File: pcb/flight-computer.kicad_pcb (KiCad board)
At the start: 4 copper layers, 74 parts, among them J1 MicroSD Slot, J2 USB_C_Receptacle_USB2.0_16P, J3 SMA_Coax, J4 Conn_01x02, J5 ARM, SW1 SW_Push, SW2 SW_Push, U1 RP2040, U10 TPS2116DRL, U11 RN2903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

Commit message: Filled out the BOM for the schematic. Consolidated some components and changed footprint sizes.
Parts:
- removed C1, C2: 15p, Capacitor_SMD:C_0402_1005Metric
- removed C10, C11, C12, C13, C14, C15, C16, C17, C19, C20, C23, C24, C25, C26, C3, C5, C6, C8, C9: 100n, Capacitor_SMD:C_0201_0603Metric
- removed C18, C30: 10u, Capacitor_SMD:C_0805_2012Metric
- removed C21: 220n, Capacitor_SMD:C_0603_1608Metric
- removed C22, C31: 4u7, Capacitor_SMD:C_0603_1608Metric
- removed C27, C4: 2u2, Capacitor_SMD:C_0603_1608Metric
- removed C28, C29, C32, C7: 1u, Capacitor_SMD:C_0603_1608Metric
- removed D1: RED LED, LED_SMD:LED_0805_2012Metric
- removed D2, D3, D4: GREEN LED, LED_SMD:LED_0805_2012Metric
- removed J1: MicroSD Slot, microsd:GCT_MEM2067-02-180-00-A_REVB
- removed J2: USB_C_Receptacle_USB2.0_16P, Connector_USB:USB_C_Receptacle_GCT_USB4105-xx-A_16P_TopMnt_Horizontal
- removed J3: SMA_Coax, Connector_Coaxial:SMA_Molex_73251-1153_EdgeMount_Horizontal
- removed J4: Conn_01x02, Connector_JST:JST_PH_S2B-PH-K_1x02_P2.00mm_Horizontal
- removed J5: ARM, TerminalBlock_Phoenix:TerminalBlock_Phoenix_MKDS-1,5-2_1x02_P5.00mm_Horizontal
- removed L1: 2u2, Inductor_SMD:L_0805_2012Metric
- removed LS1: ACTIVE BUZZER, buzzer:XDCR_AI-1223-TWT-3V-2-R
- removed R1: 11k, Resistor_SMD:R_0201_0603Metric
- removed R10, R11: 5k1, Resistor_SMD:R_0201_0603Metric
- removed R12, R13, R14, R17, R2, R9: 1k, Resistor_SMD:R_0201_0603Metric
- removed R15: 150R, Resistor_SMD:R_0201_0603Metric
- removed R16: 10k, Resistor_SMD:R_0201_0603Metric
- removed R3, R4, R5, R6: 2k2, Resistor_SMD:R_0201_0603Metric
- removed R7, R8: 27R, Resistor_SMD:R_0603_1608Metric
- removed SW1, SW2: SW_Push, Button_Switch_THT:SW_PUSH_6mm_H5mm
- removed U1: RP2040, Package_DFN_QFN:QFN-56-1EP_7x7mm_P0.4mm_EP3.2x3.2mm
- removed U10: TPS2116DRL, Package_TO_SOT_SMD:SOT-583-8
- removed U11: RN2903, RF_Module:RN2903
- removed U2: W25Q16JVSS, Package_SO:SOIC-8_5.23x5.23mm_P1.27mm
- removed U3: USBLC6-2SC6, Package_TO_SOT_SMD:SOT-23-6
- removed U4: M24C32-FMN, Package_SO:SOIC-8_3.9x4.9mm_P1.27mm
- removed U5: MS5607-02BA, Package_LGA:LGA-8_3x5mm_P1.25mm
- removed U6: LIS2MDL, Package_LGA:LGA-12_2x2mm_P0.5mm
- removed U7: LSM6DSO32TR, lsm6dso32:XDCR_LSM6DSO32TR
- removed U8: SAM-M8Q, RF_GPS:ublox_SAM-M8Q
- removed U9: LM3671MF, Package_TO_SOT_SMD:TSOT-23-5
- removed Y1: 12MHz, Crystal:Crystal_SMD_3225-4Pin_3.2x2.5mm

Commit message: Updated inductor footprint.
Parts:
- added C1: 15p, Capacitor_SMD:C_0402_1005Metric, F.Cu at (136.9, 95.7)
- added C10: 100n, Capacitor_SMD:C_0402_1005Metric, F.Cu at (139.8, 99.6)
- added C11: 100n, Capacitor_SMD:C_0402_1005Metric, F.Cu at (139.8, 101.6)
- added C12: 100n, Capacitor_SMD:C_0402_1005Metric, F.Cu at (139.8, 103.5)
- added C13: 100n, Capacitor_SMD:C_0402_1005Metric, F.Cu at (142.6, 95.7)
- added C14: 100n, Capacitor_SMD:C_0402_1005Metric, F.Cu at (142.6, 97.6)
- added C15: 100n, Capacitor_SMD:C_0402_1005Metric, F.Cu at (142.6, 99.6)
- added C16: 100n, Capacitor_SMD:C_0402_1005Metric, F.Cu at (165.2, 99.5)
- added C17: 100n, Capacitor_SMD:C_0402_1005Metric, F.Cu at (165.2, 101.4)
- added C18: 10u, Capacitor_SMD:C_0603_1608Metric, F.Cu at (166.7, 113.0)
- added C19: 100n, Capacitor_SMD:C_0402_1005Metric, F.Cu at (165.2, 103.4)
- added C2: 15p, Capacitor_SMD:C_0402_1005Metric, F.Cu at (136.9, 97.6)
- added C20: 100n, Capacitor_SMD:C_0402_1005Metric, F.Cu at (165.2, 105.4)
- added C21: 220n, Capacitor_SMD:C_0603_1608Metric, F.Cu at (166.7, 115.5)
- added C22: 4u7, Capacitor_SMD:C_0603_1608Metric, F.Cu at (166.7, 118.0)
- added C23: 100n, Capacitor_SMD:C_0402_1005Metric, F.Cu at (165.2, 107.3)
- added C24: 100n, Capacitor_SMD:C_0402_1005Metric, F.Cu at (165.2, 109.3)
- added C25: 100n, Capacitor_SMD:C_0402_1005Metric, F.Cu at (130.4, 80.1)
- added C26: 100n, Capacitor_SMD:C_0402_1005Metric, F.Cu at (130.4, 82.1)
- added C27: 4u7, Capacitor_SMD:C_0603_1608Metric, F.Cu at (131.0, 77.9)
- added C28: 1u, Capacitor_SMD:C_0603_1608Metric, F.Cu at (163.3, 64.6)
- added C29: 1u, Capacitor_SMD:C_0603_1608Metric, F.Cu at (163.3, 67.1)
- added C3: 100n, Capacitor_SMD:C_0402_1005Metric, F.Cu at (136.9, 99.6)
- added C30: 10u, Capacitor_SMD:C_0603_1608Metric, F.Cu at (163.3, 69.7)
- added C31: 4u7, Capacitor_SMD:C_0603_1608Metric, F.Cu at (163.3, 72.2)
- added C32: 1u, Capacitor_SMD:C_0603_1608Metric, F.Cu at (163.3, 74.7)
- added C4: 2u2, Capacitor_SMD:C_0603_1608Metric, F.Cu at (137.5, 105.8)
- added C5: 100n, Capacitor_SMD:C_0402_1005Metric, F.Cu at (136.9, 101.6)
- added C6: 100n, Capacitor_SMD:C_0402_1005Metric, F.Cu at (136.9, 103.5)
- added C7: 1u, Capacitor_SMD:C_0603_1608Metric, F.Cu at (137.5, 108.3)
- added C8: 100n, Capacitor_SMD:C_0402_1005Metric, F.Cu at (139.8, 95.7)
- added C9: 100n, Capacitor_SMD:C_0402_1005Metric, F.Cu at (139.8, 97.6)
- added D1: RED LED, LED_SMD:LED_0805_2012Metric, F.Cu at (110.2, 122.6)
- added D2: GREEN LED, LED_SMD:LED_0805_2012Metric, F.Cu at (110.2, 125.6)
- added D3: GREEN LED, LED_SMD:LED_0805_2012Metric, F.Cu at (110.2, 128.7)
- added D4: GREEN LED, LED_SMD:LED_0805_2012Metric, F.Cu at (167.5, 69.5)
- added J1: MicroSD Slot, microsd:GCT_MEM2067-02-180-00-A_REVB, F.Cu at (127.0, 102.7)
- added J2: USB_C_Receptacle_USB2.0_16P, Connector_USB:USB_C_Receptacle_GCT_USB4105-xx-A_16P_TopMnt_Horizontal, F.Cu at (138.7, 127.9)
- added J3: SMA_Coax, Connector_Coaxial:SMA_Molex_73251-1153_EdgeMount_Horizontal, F.Cu at (143.8, 70.0)
- added J4: Conn_01x02, Connector_JST:JST_PH_S2B-PH-K_1x02_P2.00mm_Horizontal, F.Cu at (164.2, 78.3)
- added J5: ARM, TerminalBlock_Phoenix:TerminalBlock_Phoenix_MKDS-3-2-5.08_1x02_P5.08mm_Horizontal, F.Cu at (152.6, 70.3)
- added L1: 2u2, LPO3310-222MLC:LPO3310222MLC, F.Cu at (152.7, 80.1)
- added LS1: ACTIVE BUZZER, buzzer:XDCR_AI-1223-TWT-3V-2-R, F.Cu at (126.0, 117.4)
- added R1: 11k, Resistor_SMD:R_0402_1005Metric, F.Cu at (134.3, 111.7)
- added R10: 5k1, Resistor_SMD:R_0402_1005Metric, F.Cu at (137.2, 117.6)
- added R11: 5k1, Resistor_SMD:R_0402_1005Metric, F.Cu at (137.2, 119.6)
- added R12: 100R, Resistor_SMD:R_0402_1005Metric, F.Cu at (137.2, 121.6)
- added R13: 68R, Resistor_SMD:R_0402_1005Metric, F.Cu at (140.1, 111.7)
- added R14: 68R, Resistor_SMD:R_0402_1005Metric, F.Cu at (140.1, 113.6)
- added R15: 150R, Resistor_SMD:R_0402_1005Metric, F.Cu at (140.1, 115.6)
- added R16: 11k, Resistor_SMD:R_0402_1005Metric, F.Cu at (166.7, 72.0)
- added R17: 68R, Resistor_SMD:R_0402_1005Metric, F.Cu at (166.7, 74.0)
- added R2: 1k, Resistor_SMD:R_0402_1005Metric, F.Cu at (134.3, 113.6)
- added R3: 2k2, Resistor_SMD:R_0402_1005Metric, F.Cu at (134.3, 115.6)
- added R4: 2k2, Resistor_SMD:R_0402_1005Metric, F.Cu at (134.3, 117.6)
- added R5: 2k2, Resistor_SMD:R_0402_1005Metric, F.Cu at (134.3, 119.6)
- added R6: 2k2, Resistor_SMD:R_0402_1005Metric, F.Cu at (134.3, 121.6)
- added R7: 27R, Resistor_SMD:R_0402_1005Metric, F.Cu at (137.2, 111.7)
- added R8: 27R, Resistor_SMD:R_0402_1005Metric, F.Cu at (137.2, 113.6)
- added R9: 1k, Resistor_SMD:R_0402_1005Metric, F.Cu at (137.2, 115.6)
- added SW1: SW_Push, Button_Switch_THT:SW_PUSH_6mm_H5mm, F.Cu at (110.0, 96.7)
- added SW2: SW_Push, Button_Switch_THT:SW_PUSH_6mm_H5mm, F.Cu at (110.0, 105.2)
- added U1: RP2040, Package_DFN_QFN:QFN-56-1EP_7x7mm_P0.4mm_EP3.2x3.2mm, F.Cu at (112.6, 116.4)
- added U10: LM3671MF, Package_TO_SOT_SMD:TSOT-23-5, F.Cu at (167.9, 65.8)
- added U11: TPS2116DRL, Package_TO_SOT_SMD:SOT-583-8, F.Cu at (158.1, 78.6)
- added U2: W25Q16JVSS, Package_SO:SOIC-8_5.23x5.23mm_P1.27mm, F.Cu at (123.7, 127.6)
- added U3: USBLC6-2SC6, Package_TO_SOT_SMD:SOT-23-6, F.Cu at (115.0, 127.9)
- added U4: M24C32-FMN, Package_SO:SOIC-8_3.9x4.9mm_P1.27mm, F.Cu at (150.7, 115.1)
- added U5: MS5607-02BA, Package_LGA:LGA-8_3x5mm_P1.25mm, F.Cu at (162.4, 115.2)
- added U6: LIS2MDL, Package_LGA:LGA-12_2x2mm_P0.5mm, F.Cu at (165.8, 96.7)
- added U7: LSM6DSO32TR, lsm6dso32:XDCR_LSM6DSO32TR, F.Cu at (157.7, 113.8)
- added U8: SAM-M8Q, RF_GPS:ublox_SAM-M8Q, F.Cu at (155.3, 103.2)
- added U9: RN2903, RF_Module:RN2903, F.Cu at (118.5, 78.4)
- added Y1: 12MHz, Crystal:Crystal_SMD_3225-4Pin_3.2x2.5mm, F.Cu at (115.0, 123.3)

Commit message: Initial layout
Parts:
- moved R3 68.5 mm to (158.4, 51.5)
- moved R4 68.5 mm to (158.4, 53.6)
- moved R5 68.5 mm to (158.4, 55.6)
- moved R6 68.5 mm to (158.4, 57.5)
- moved U9 52.4 mm to (169.0, 92.3), turned to -90 degrees
- moved R16 51.9 mm to (117.8, 89.4), turned to 90 degrees
- moved J4 49.9 mm to (114.9, 85.8), turned to -90 degrees
- moved D3 49.7 mm to (136.0, 86.2), turned to -90 degrees
- moved C28 49.5 mm to (118.7, 86.1), turned to 90 degrees
- moved C29 48.9 mm to (121.1, 91.9)
- moved J3 48.8 mm to (186.8, 93.2), turned to 180 degrees
- moved C19 46.2 mm to (121.0, 116.5), turned to 90 degrees
- moved D2 45.5 mm to (132.9, 86.2), turned to -90 degrees
- moved C26 45.0 mm to (170.2, 103.2), turned to 180 degrees
- moved U7 44.6 mm to (163.2, 69.5), turned to 180 degrees
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
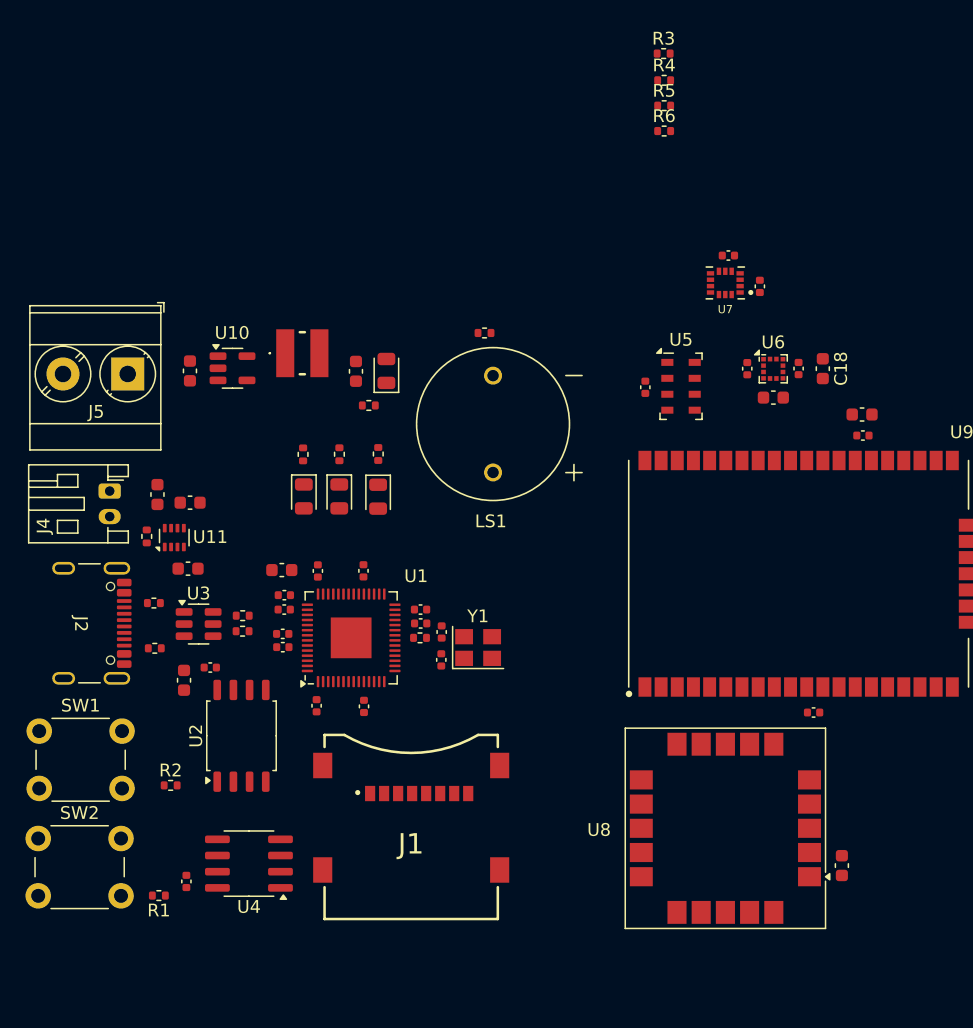
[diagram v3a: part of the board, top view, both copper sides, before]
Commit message: Updated GPS to L86G
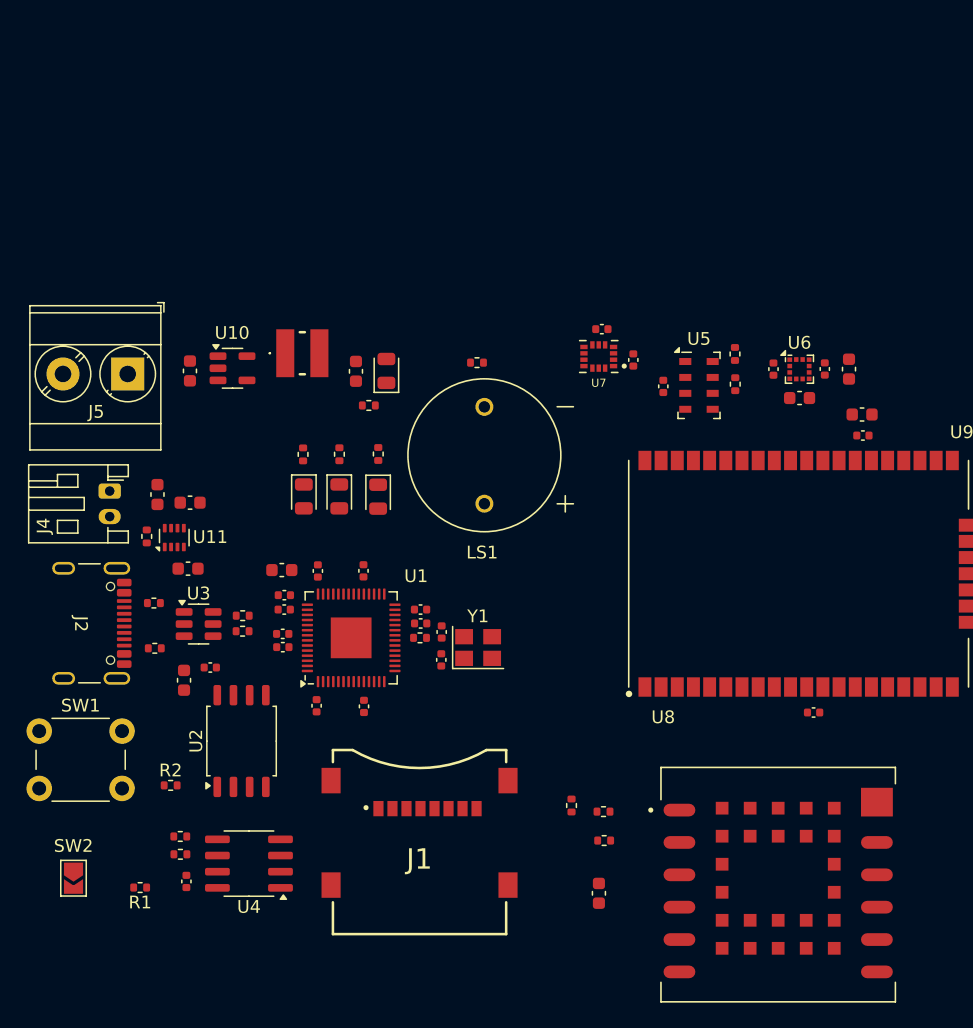
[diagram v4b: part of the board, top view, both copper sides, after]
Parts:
- added R18: 1k, Resistor_SMD:R_0402_1005Metric, F.Cu at (153.7, 111.0)
- added R19: 1k, Resistor_SMD:R_0402_1005Metric, F.Cu at (153.7, 113.2)
- added R20: 5k6, Resistor_SMD:R_0402_1005Metric, F.Cu at (151.2, 110.5)
- SW2: footprint Button_Switch_THT:SW_PUSH_6mm_H5mm -> Jumper:SolderJumper-2_P1.3mm_Open_TrianglePad1.0x1.5mm
- U8: value SAM-M8Q -> LC86G; footprint RF_GPS:ublox_SAM-M8Q -> LC86G:XCVR_LC86G
- moved R5 68.8 mm to (120.5, 112.9)
- moved R6 68.3 mm to (120.5, 114.3)
- moved R3 26.6 mm to (164.0, 77.4), turned to 90 degrees
- moved R4 22.2 mm to (164.0, 75.0), turned to -90 degrees
- moved C22 19.2 mm to (153.3, 117.4), turned to 90 degrees
- moved U7 11.5 mm to (153.3, 75.2)
- moved C23 11.5 mm to (153.6, 73.1)
- moved C24 11.5 mm to (156.0, 75.5)
- moved U8 6.06 mm to (167.4, 116.7), turned to 0 degrees
- moved SW2 4.17 mm to (112.1, 116.2), turned to -90 degrees
- moved LS1 2.54 mm to (144.3, 83.0)
- moved R15 2.40 mm to (143.8, 75.7)
- moved C16 2.06 mm to (171.1, 76.2)
- moved C17 2.06 mm to (167.0, 76.2)
- moved C18 2.06 mm to (173.0, 76.2)
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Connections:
- U8 pad 1: GND -> Net-(U8-RXD)
- U8 pad 10: GND -> unconnected-(U8-~{RESET}-Pad10)
- U8 pad 11: GND -> unconnected-(U8-EX_ANT-Pad11)
- U8 pad 12: unconnected-(U8-SCL-Pad12) -> GND
- U8 pad 13: MCU_UART0_RX -> GND
- U8 pad 14: MCU_UART0_TX -> GND
- U8 pad 17: +3V3 -> GND
- U8 pad 18: RST_N -> GND
- U8 pad 19: unconnected-(U8-EXTINT-Pad19) -> GND
- U8 pad 2: +3V3 -> Net-(U8-TXD)
- U8 pad 3: +3V3 -> GND
- U8 pad 4: GND -> +3V3
- U8 pad 5: GND -> +3V3
- U8 pad 6: GND -> unconnected-(U8-1PPS-Pad6)

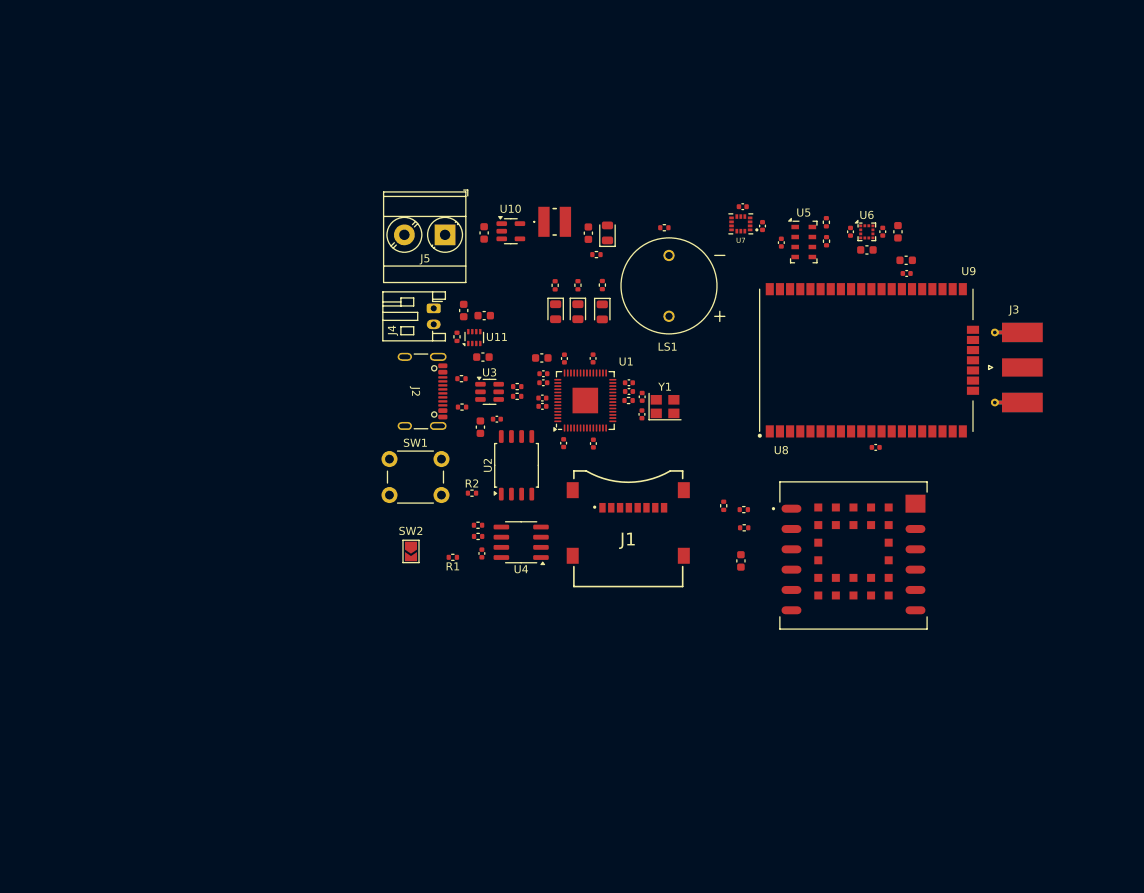
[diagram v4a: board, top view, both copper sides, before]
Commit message: Added mounting holes and copper pours.
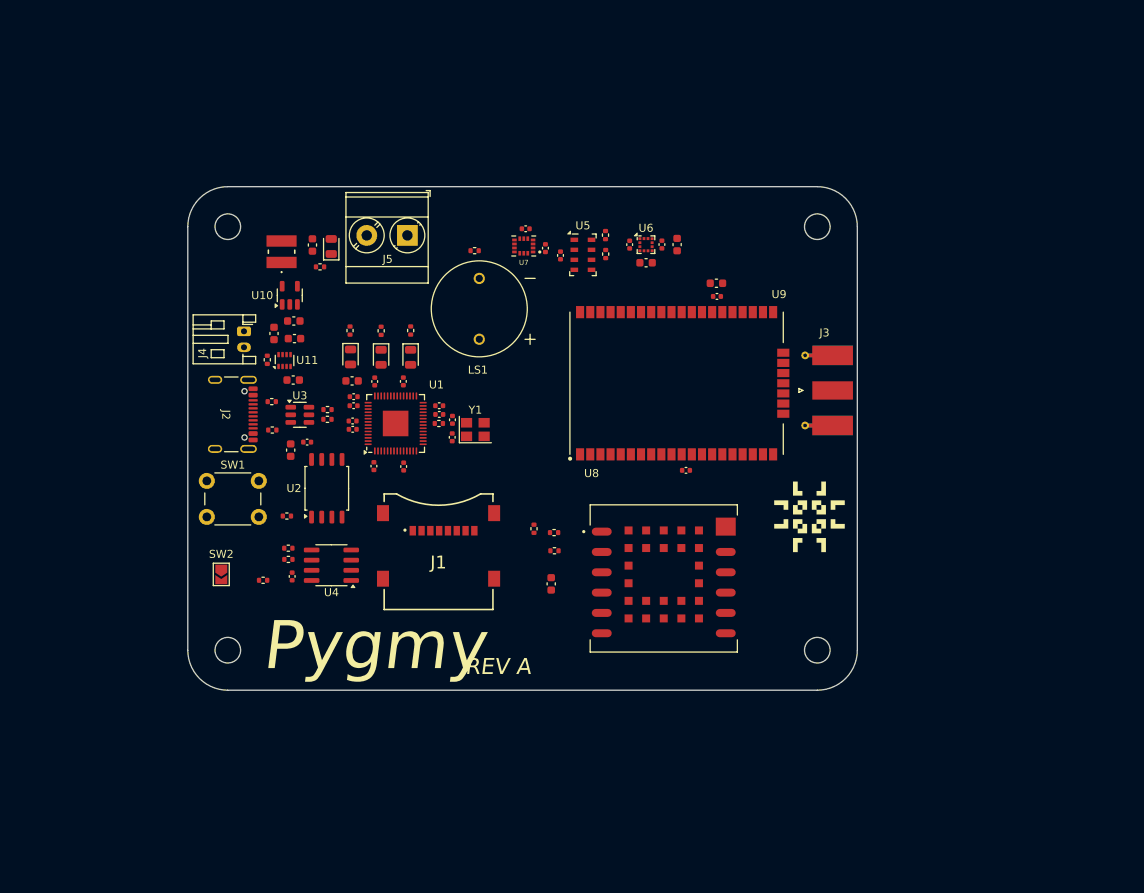
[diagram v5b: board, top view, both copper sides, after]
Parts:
- added G***: LOGO, Logos:PulsarLogo_10mm, F.Cu at (161.9, 111.9)
- added H1: MountingHole, MountingHole:MountingHole_3.2mm_M3, F.Cu at (162.9, 75.6)
- added H2: MountingHole, MountingHole:MountingHole_3.2mm_M3, F.Cu at (162.9, 128.5)
- added H3: MountingHole, MountingHole:MountingHole_3.2mm_M3, F.Cu at (89.2, 128.5)
- added H4: MountingHole, MountingHole:MountingHole_3.2mm_M3, F.Cu at (89.2, 75.6)
- moved R17 34.6 mm to (100.7, 80.6)
- moved D4 34.6 mm to (102.1, 78.1)
- moved C30 34.5 mm to (99.8, 77.9)
- moved L1 34.3 mm to (95.9, 78.7), turned to 90 degrees
- moved U10 28.8 mm to (96.9, 84.2), turned to 90 degrees
- moved C18 27.7 mm to (145.4, 77.8)
- moved C21 27.7 mm to (141.5, 80.1)
- moved C16 27.7 mm to (143.5, 77.8)
- moved C17 27.7 mm to (139.4, 77.8)
- moved C20 27.7 mm to (130.8, 79.2)
- moved R3 27.7 mm to (136.4, 79.0)
- moved R4 27.7 mm to (136.4, 76.7)
- moved U5 27.7 mm to (133.6, 79.1)
- moved U6 27.7 mm to (141.5, 77.8)
- moved C23 27.3 mm to (126.4, 75.9)
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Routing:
- added copper zone on In2.Cu, net +3V3
- added copper zone on In1.Cu, net GND
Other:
- board outline added: 83.7 x 62.9 mm
- board text added: "Pygmy"
- board text added: "REV A"
